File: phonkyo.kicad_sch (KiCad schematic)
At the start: 30 parts, among them J1 GPIO, J2 LineOutJack, J4 RIJack, U1 CAT24C256, U2 PCM5102A, U3 XC6206P332MR

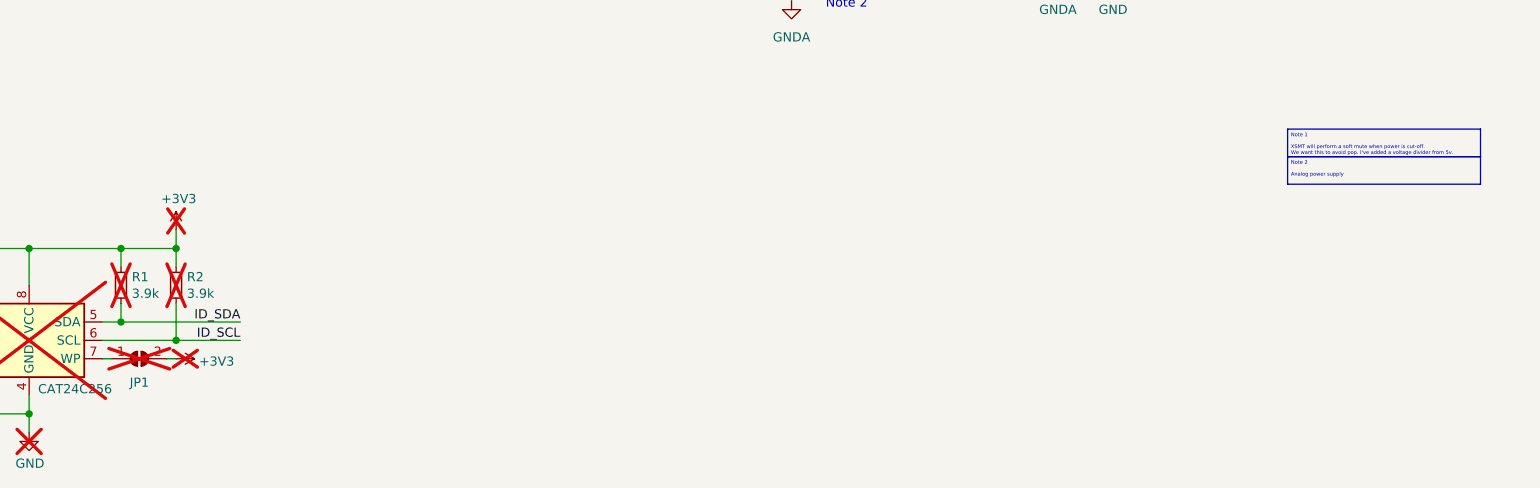
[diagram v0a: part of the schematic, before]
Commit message: chore: convert design to KiCad 10 format
Upgrades the schematic and board with kicad-cli 10.0.6:

  phonkyo.kicad_sch  20231120 (8.0) -> 20260306 (10.0)
  phonkyo.kicad_pcb  20240108 (8.0) -> 20260206 (10.0)

The files will no longer open in KiCad 8 or 9.

The text diff is ~31k lines because KiCad re-serialises the whole file,
so it cannot be reviewed by reading. The conversion was verified instead
by exporting from KiCad 10 before and after and comparing the outputs:

- Netlist: 25 components, 45 nets, 111 pin connections, identical.
- Gerbers and drill: 28 of 30 files identical after stripping comments
  and dates. F_Silkscreen and Edge_Cuts differ in text but are
  geometrically identical when replayed. Apertures D10/D11 were
  renumbered and the outline segments were reordered.
- ERC 57 and DRC 23 findings, identical by type before and after.
- DRC reports 0 unconnected items and 0 schematic-parity errors.

phonkyo.kicad_prl is included because KiCad 10 migrates it (layer
visibility and opacity keys). It holds only per-user UI state.

.kicad_pro did not change. production/ is historical fabrication
output and was not regenerated.

Co-Authored-By: Claude Opus 5.5 <noreply@anthropic.com>
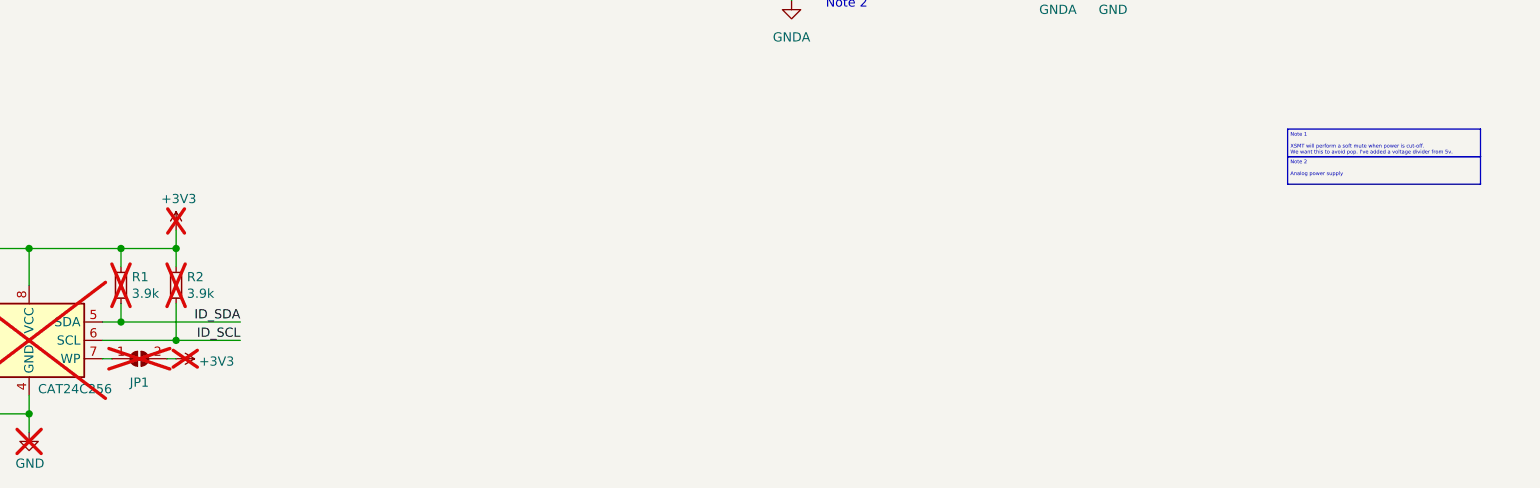
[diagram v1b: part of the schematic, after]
